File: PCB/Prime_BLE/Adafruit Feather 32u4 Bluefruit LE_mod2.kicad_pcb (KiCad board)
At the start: 2 copper layers, 362.5 x 94.5 mm, 175 parts, among them J1 JTAG_ITF, J2 Conn_01x02, K1 KEYSW, K10 KEYSW, K11 KEYSW, K12 KEYSW, K13 KEYSW, K14 KEYSW, K15 KEYSW, K16 KEYSW, K17 KEYSW, K18 KEYSW, K19 KEYSW, K2 KEYSW, K20 KEYSW, K21 KEYSW, K22 KEYSW, K23 KEYSW, K24 KEYSW, K25 KEYSW, K26 KEYSW, K27 KEYSW, K28 KEYSW, K29 KEYSW, K3 KEYSW, K30 KEYSW, K31 KEYSW, K32 KEYSW, K33 KEYSW, K34 KEYSW, K35 KEYSW, K36 KEYSW, K37 KEYSW, K38 KEYSW, K39 KEYSW, K4 KEYSW, K40 KEYSW, K41 KEYSW, K42 KEYSW, K43 KEYSW, K44 KEYSW, K45 KEYSW, K46 KEYSW, K47 KEYSW, K48 KEYSW, K49 KEYSW, K5 KEYSW, K50 KEYSW, K51 KEYSW, K52 KEYSW, K53 KEYSW, K54 KEYSW, K55 KEYSW, K56 KEYSW, K57 KEYSW, K6 KEYSW, K7 KEYSW, K8 KEYSW, K9 KEYSW, SW1 SW_PUSH, SW2 SW_PUSH, SW3 SW_PUSH, SW4 SW_SPDT, U1 MBT40, U2 MCP73831-2-OT, U3 MIC5219-3.3YM5, U4 ATmega32U4-AU, X1 JSTPH, X2 JTAG-CORTEXBOXPOSTS, Y1 8MHz

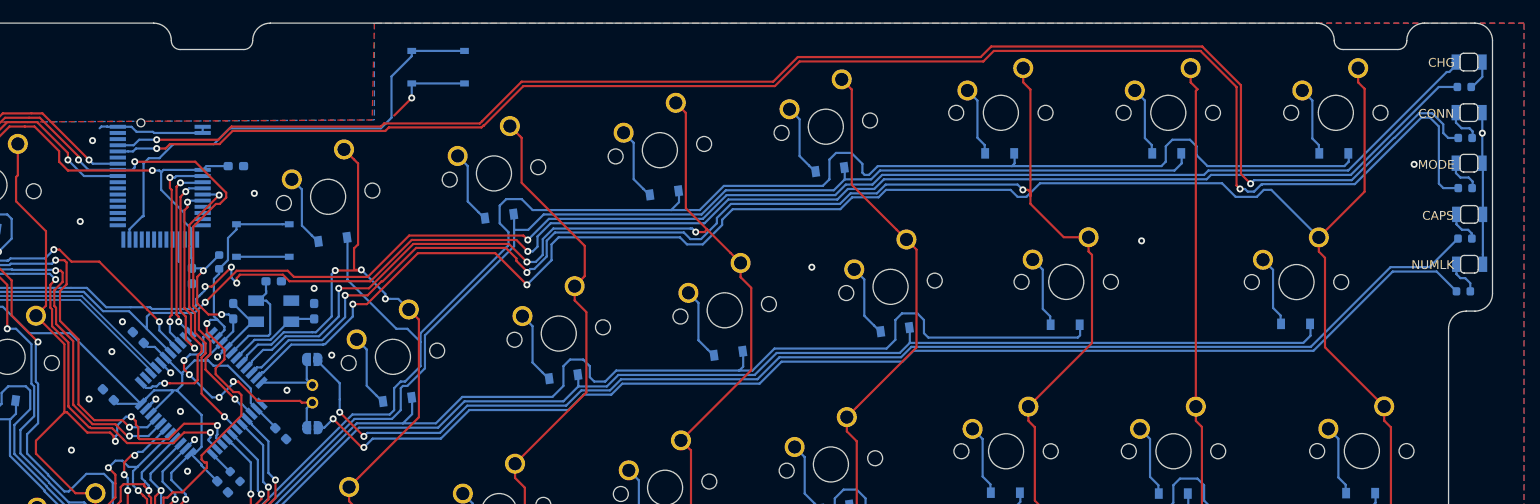
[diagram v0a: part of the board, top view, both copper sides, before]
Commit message: fixed issues detailed in the master branch readme
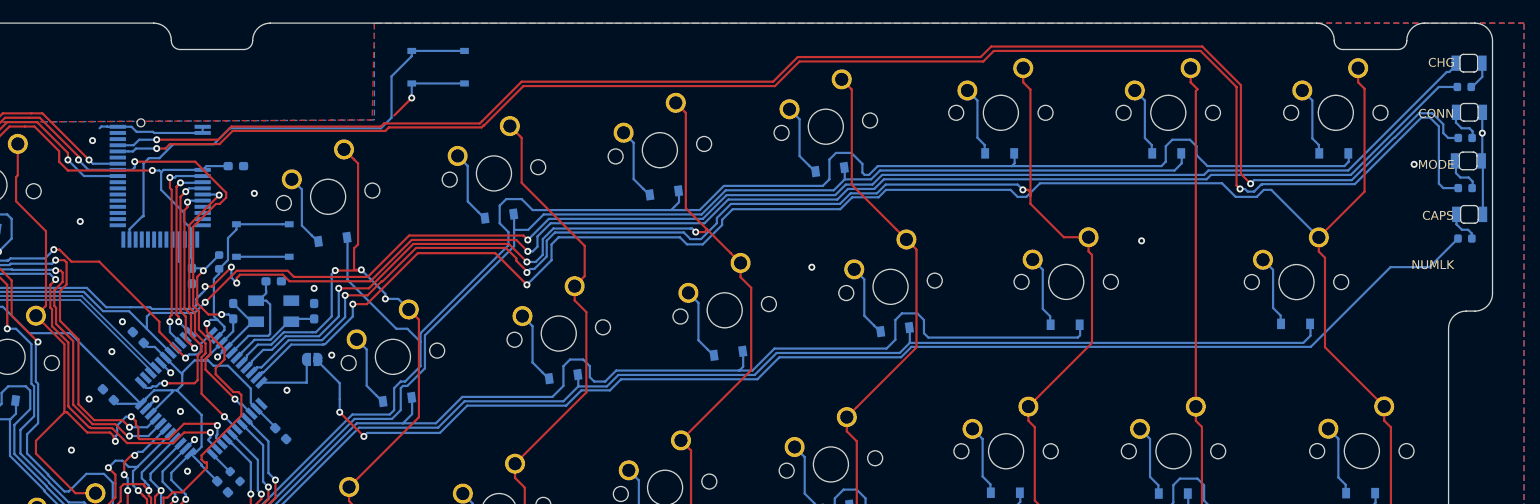
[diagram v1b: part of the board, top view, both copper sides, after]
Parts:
- removed CHG1: ORANGE, Adafruit Feather 32u4 Bluefruit LE:IN-S124BR_LED
- removed J2: Conn_01x02, Connector_PinSocket_2.00mm:PinSocket_1x02_P2.00mm_Vertical
- removed JP2: SolderJumper_2_Open, Jumper:SolderJumper-2_P1.3mm_Open_RoundedPad1.0x1.5mm
- removed R12: 1k, Resistor_SMD:R_0603_1608Metric
- D1: value RED -> LED
- D2: value BLUE -> LED
- R1: value 2.2K -> 2.2k
- R11: value 1k -> 2.2k
- R2: value 1K -> 2.2k
- moved D67 22.9 mm to (394.7, 109.9)
- moved D1 0.28 mm to (394.7, 121.0)
- moved D2 0.05 mm to (394.8, 115.5)
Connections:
- D1 pad 1: (no net) -> GND
- D1 pad 2: (no net) -> Net-(D1-Pad2)
- D2 pad 1: (no net) -> GND
- D2 pad 2: (no net) -> Net-(D2-Pad2)
- D67 pad 1: GND -> Net-(D67-Pad1)
- D67 pad 2: Net-(D67-Pad2) -> VBUS
- R1 pad 2: Net-(D1-PadA) -> Net-(D1-Pad2)
- R10 pad 2: Net-(D2-PadA) -> Net-(D2-Pad2)
- R2 pad 1: Net-(CHG1-PadC) -> Net-(D67-Pad1)
- U4 pad 12: /NUML -> /Col0
- U4 pad 8: /Col0 -> Net-(U4-Pad8)
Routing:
- net Net-(JP2-Pad2): track 140.4 -> 0.00 mm, vias 2 -> 0
- net /NUML: track 27.3 -> 0.00 mm, vias 4 -> 0
- net /Col0: track 330.7 -> 337.0 mm
- net GND: track 134.4 -> 128.5 mm
- net Net-(D2-PadA): track 4.19 -> 0.00 mm
- net Net-(D2-Pad2): track 0.00 -> 4.19 mm
- net Net-(D1-PadA): track 4.17 -> 0.00 mm
- net Net-(D1-Pad2): track 0.00 -> 4.17 mm
- net Net-(D67-Pad2): track 4.05 -> 0.00 mm
- net Net-(D67-Pad1): track 0.00 -> 3.36 mm
- net Net-(CHG1-PadC): track 3.36 -> 0.00 mm
- net /CAPS: track 8.83 -> 7.53 mm
